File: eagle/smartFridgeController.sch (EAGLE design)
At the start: 12 parts

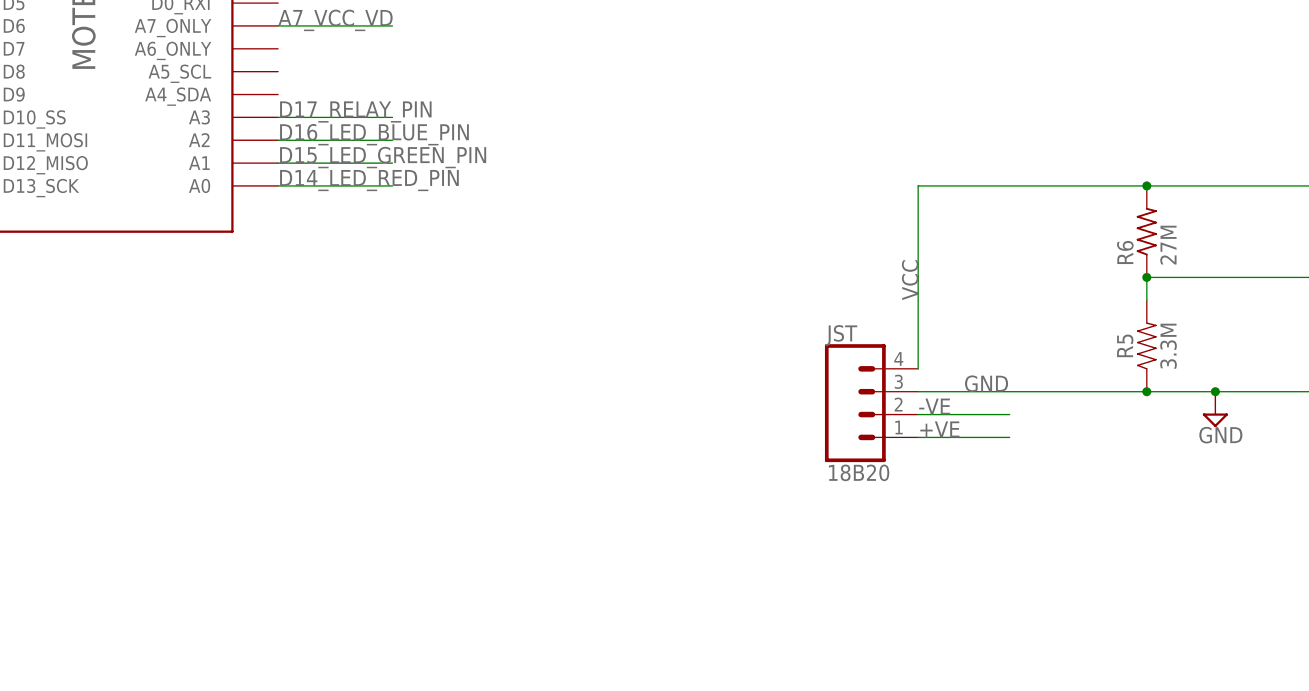
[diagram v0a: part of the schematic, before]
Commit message: gnd, vcc switch, labled switch on oki-78
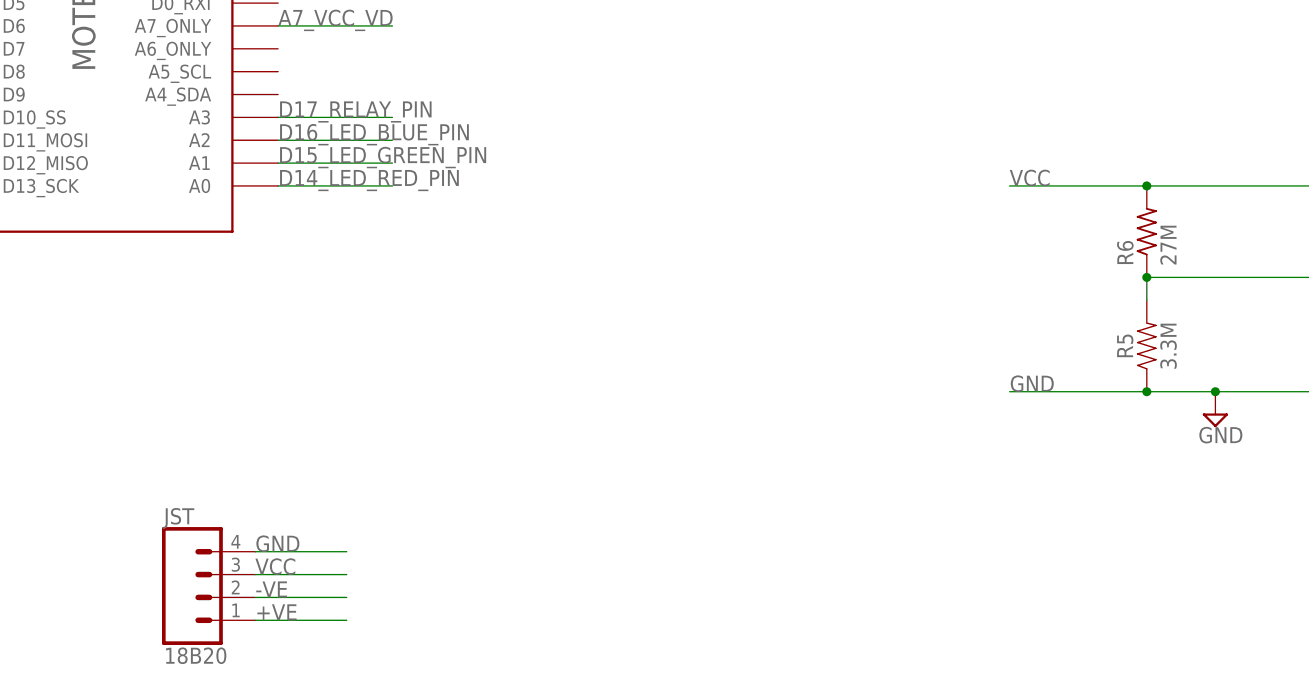
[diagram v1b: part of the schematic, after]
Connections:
- new net N$4: JST.4
- net GND: no longer JST.3
- net VCC: now also JST.3; no longer JST.4
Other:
- moved on the sheet: JST
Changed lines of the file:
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@@
 <instance part="C1" gate="G$1" x="190.5" y="50.8"/>
 <instance part="R5" gate="G$1" x="170.18" y="50.8" rot="R90"/>
-<instance part="JST" gate="G$1" x="139.7" y="43.18"/>
+<instance part="JST" gate="G$1" x="66.04" y="22.86"/>
 <instance part="R6" gate="G$1" x="170.18" y="63.5" rot="R90"/>
 <instance part="SUPPLY3" gate="GND" x="93.98" y="96.52"/>
@@
 <segment>
 <pinref part="C1" gate="G$1" pin="2"/>
-<wire x1="144.78" y1="45.72" x2="170.18" y2="45.72" width="0.1524" layer="91"/>
 <wire x1="170.18" y1="45.72" x2="177.8" y2="45.72" width="0.1524" layer="91"/>
 <wire x1="177.8" y1="45.72" x2="190.5" y2="45.72" width="0.1524" layer="91"/>
 <wire x1="190.5" y1="45.72" x2="190.5" y2="48.26" width="0.1524" layer="91"/>
-<label x="149.86" y="45.72" size="1.778" layer="95"/>
+<label x="71.12" y="27.94" size="1.778" layer="95"/>
 <pinref part="R5" gate="G$1" pin="1"/>
-<junction x="170.18" y="45.72"/>
 <pinref part="SUPPLY7" gate="GND" pin="GND"/>
 <junction x="177.8" y="45.72"/>
 <wire x1="190.5" y1="45.72" x2="231.14" y2="45.72" width="0.1524" layer="91"/>
 <junction x="190.5" y="45.72"/>
-<pinref part="JST" gate="G$1" pin="3"/>
 <pinref part="OKI-78SR-5/1.5-W36-C" gate="J$1" pin="3"/>
 <wire x1="231.14" y1="53.34" x2="231.14" y2="45.72" width="0.1524" layer="91"/>
+<wire x1="170.18" y1="45.72" x2="154.94" y2="45.72" width="0.1524" layer="91"/>
+<junction x="170.18" y="45.72"/>
+<label x="154.94" y="45.72" size="1.778" layer="95"/>
 </segment>
 <segment>
@@
 <net name="VCC" class="1">
 <segment>
-<wire x1="144.78" y1="68.58" x2="144.78" y2="48.26" width="0.1524" layer="91"/>
-<label x="144.78" y="55.88" size="1.778" layer="95" rot="R90"/>
-<pinref part="JST" gate="G$1" pin="4"/>
-<wire x1="144.78" y1="68.58" x2="170.18" y2="68.58" width="0.1524" layer="91"/>
 <pinref part="R6" gate="G$1" pin="2"/>
 <wire x1="170.18" y1="68.58" x2="223.52" y2="68.58" width="0.1524" layer="91"/>
-<junction x="170.18" y="68.58"/>
 <wire x1="223.52" y1="68.58" x2="223.52" y2="58.42" width="0.1524" layer="91"/>
 <pinref part="OKI-78SR-5/1.5-W36-C" gate="J$1" pin="1"/>
 <wire x1="223.52" y1="58.42" x2="231.14" y2="58.42" width="0.1524" layer="91"/>
+<wire x1="170.18" y1="68.58" x2="154.94" y2="68.58" width="0.1524" layer="91"/>
+<junction x="170.18" y="68.58"/>
+<label x="154.94" y="68.58" size="1.778" layer="95"/>
+</segment>
+<segment>
+<pinref part="JST" gate="G$1" pin="3"/>
+<wire x1="71.12" y1="25.4" x2="81.28" y2="25.4" width="0.1524" layer="91"/>
+<label x="71.12" y="25.4" size="1.778" layer="95"/>
 </segment>
 </net>
@@
 <segment>
 <pinref part="JST" gate="G$1" pin="1"/>
-<wire x1="144.78" y1="40.64" x2="154.94" y2="40.64" width="0.1524" layer="91"/>
-<label x="144.78" y="40.64" size="1.778" layer="95"/>
+<wire x1="71.12" y1="20.32" x2="81.28" y2="20.32" width="0.1524" layer="91"/>
+<label x="71.12" y="20.32" size="1.778" layer="95"/>
 </segment>
 <segment>
@@
 <segment>
 <pinref part="JST" gate="G$1" pin="2"/>
-<wire x1="144.78" y1="43.18" x2="154.94" y2="43.18" width="0.1524" layer="91"/>
-<label x="144.78" y="43.18" size="1.778" layer="95"/>
+<wire x1="71.12" y1="22.86" x2="81.28" y2="22.86" width="0.1524" layer="91"/>
+<label x="71.12" y="22.86" size="1.778" layer="95"/>
 </segment>
 <segment>
@@
 </segment>
 </net>
+<net name="N$4" class="0">
+<segment>
+<pinref part="JST" gate="G$1" pin="4"/>
+<wire x1="71.12" y1="27.94" x2="81.28" y2="27.94" width="0.1524" layer="91"/>
+</segment>
+</net>

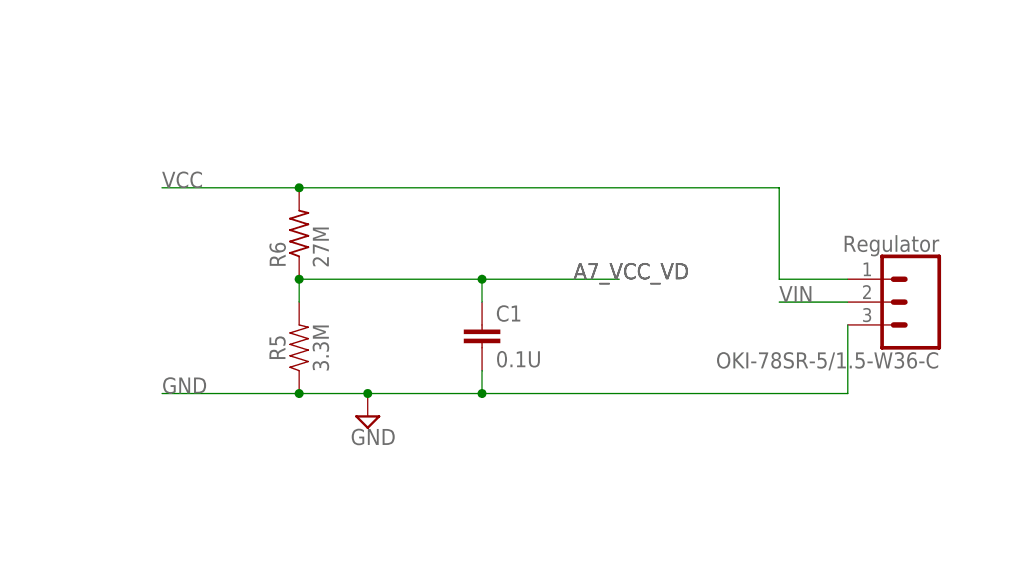
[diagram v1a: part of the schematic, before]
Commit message: silkscreen fixes, routing 0.3
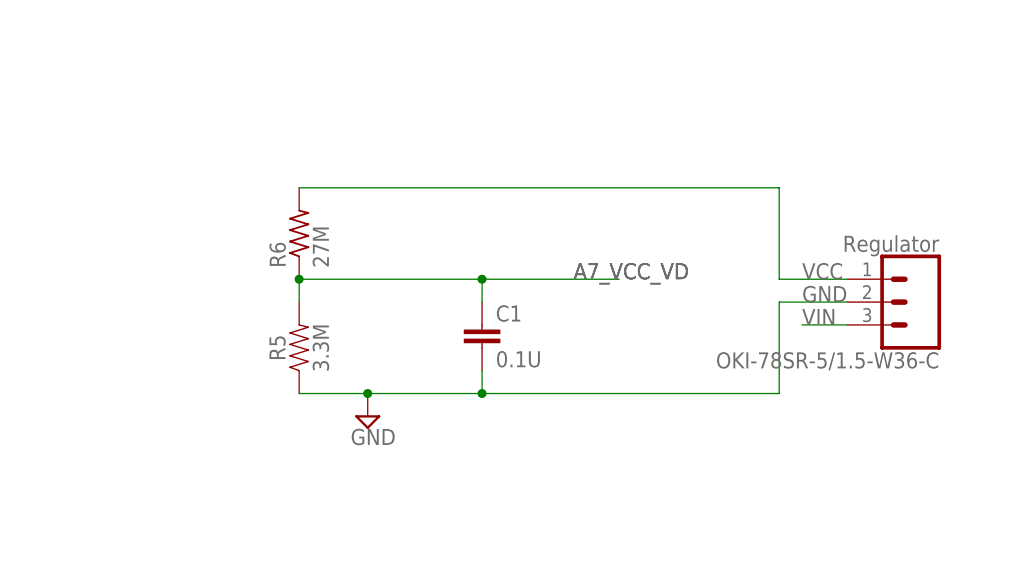
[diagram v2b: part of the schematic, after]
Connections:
- net GND: now also OKI-78SR-5/1.5-W36-C.2; no longer OKI-78SR-5/1.5-W36-C.3
- net VIN: now also OKI-78SR-5/1.5-W36-C.3; no longer OKI-78SR-5/1.5-W36-C.2
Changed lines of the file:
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@@
 <pinref part="SUPPLY7" gate="GND" pin="GND"/>
 <junction x="177.8" y="45.72"/>
-<wire x1="190.5" y1="45.72" x2="231.14" y2="45.72" width="0.1524" layer="91"/>
+<wire x1="190.5" y1="45.72" x2="223.52" y2="45.72" width="0.1524" layer="91"/>
+<wire x1="223.52" y1="45.72" x2="223.52" y2="55.88" width="0.1524" layer="91"/>
 <junction x="190.5" y="45.72"/>
-<pinref part="OKI-78SR-5/1.5-W36-C" gate="J$1" pin="3"/>
-<wire x1="231.14" y1="53.34" x2="231.14" y2="45.72" width="0.1524" layer="91"/>
-<wire x1="170.18" y1="45.72" x2="154.94" y2="45.72" width="0.1524" layer="91"/>
-<junction x="170.18" y="45.72"/>
-<label x="154.94" y="45.72" size="1.778" layer="95"/>
+<pinref part="OKI-78SR-5/1.5-W36-C" gate="J$1" pin="2"/>
+<wire x1="223.52" y1="55.88" x2="231.14" y2="55.88" width="0.1524" layer="91"/>
+<label x="226.06" y="55.88" size="1.778" layer="95"/>
 </segment>
 <segment>
@@
 </segment>
 <segment>
-<pinref part="OKI-78SR-5/1.5-W36-C" gate="J$1" pin="2"/>
-<wire x1="231.14" y1="55.88" x2="223.52" y2="55.88" width="0.1524" layer="91"/>
-<label x="223.52" y="55.88" size="1.778" layer="95"/>
+<pinref part="OKI-78SR-5/1.5-W36-C" gate="J$1" pin="3"/>
+<wire x1="231.14" y1="53.34" x2="226.06" y2="53.34" width="0.1524" layer="91"/>
+<label x="226.06" y="53.34" size="1.778" layer="95"/>
 </segment>
 </net>
@@
 <pinref part="OKI-78SR-5/1.5-W36-C" gate="J$1" pin="1"/>
 <wire x1="223.52" y1="58.42" x2="231.14" y2="58.42" width="0.1524" layer="91"/>
-<wire x1="170.18" y1="68.58" x2="154.94" y2="68.58" width="0.1524" layer="91"/>
-<junction x="170.18" y="68.58"/>
-<label x="154.94" y="68.58" size="1.778" layer="95"/>
+<label x="226.06" y="58.42" size="1.778" layer="95"/>
 </segment>
 <segment>

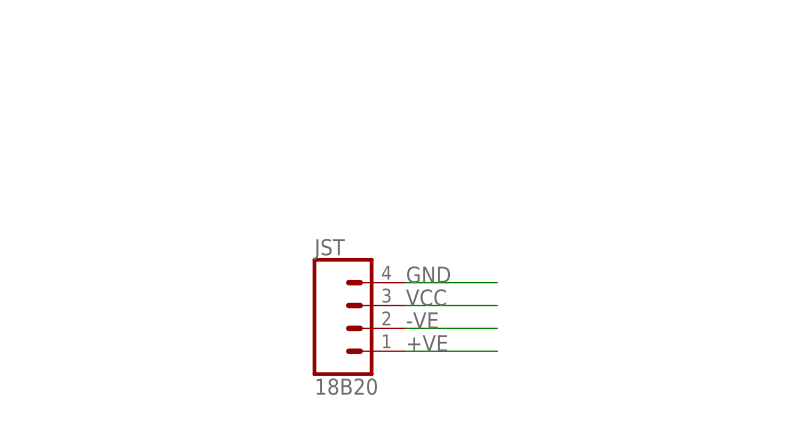
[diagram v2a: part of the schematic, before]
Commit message: Moved to screwterminal(s)
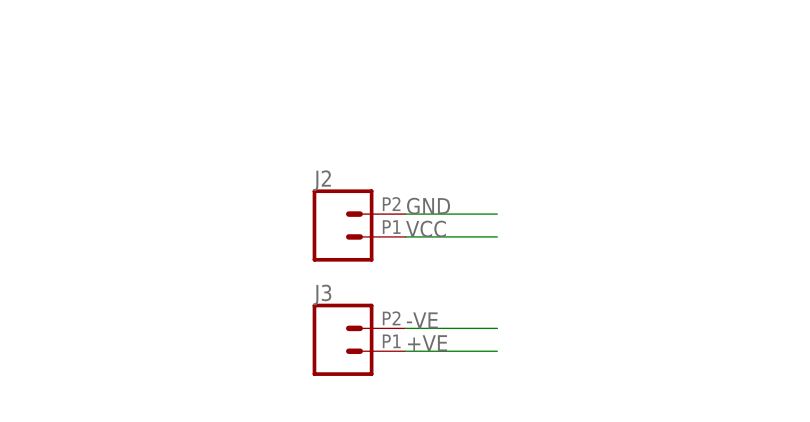
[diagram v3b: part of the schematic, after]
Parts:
- removed JST: 18B20, SparkFun-Connectors:CONN_04JST-PTH
- added J2, J3: (no value), SparkFun-Connectors:CONN_022.54MM_SCREWTERM
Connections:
- removed net N$4: JST.4
- net +VE: now also J3.1; no longer JST.1
- net -VE: now also J3.2; no longer JST.2
- net GND: now also J2.2
- net VCC: now also J2.1; no longer JST.3
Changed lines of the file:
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@@
 <part name="C1" library="SparkFun-Capacitors" deviceset="0.1UF" device="-KIT-EZ-50V-20%" value="0.1U"/>
 <part name="R5" library="SparkFun-Resistors" deviceset="1KOHM" device="-HORIZ-1/4W-1%" value="3.3M"/>
-<part name="JST" library="SparkFun-Connectors" deviceset="CONN_04" device="JST-PTH" value="18B20"/>
 <part name="R6" library="adafruit" deviceset="R-US_" device="0309/12" value="27M"/>
 <part name="SUPPLY3" library="supply2" deviceset="GND" device=""/>
@@
 <part name="IXYS_CPC_1706Y" library="relay" library_urn="urn:adsk.eagle:library:339" deviceset="AQZ10*D" device="" package3d_urn="urn:adsk.eagle:package:24370/1" technology="2"/>
 <part name="STATUS_LED" library="SparkFun-LED" deviceset="LED-RGB-CA" device="CLEAR" value="CLEAR"/>
+<part name="J2" library="SparkFun-Connectors" deviceset="CONN_02" device="2.54MM_SCREWTERM"/>
+<part name="J3" library="SparkFun-Connectors" deviceset="CONN_02" device="2.54MM_SCREWTERM"/>
 </parts>
 <sheets>
@@
 <instance part="C1" gate="G$1" x="190.5" y="50.8"/>
 <instance part="R5" gate="G$1" x="170.18" y="50.8" rot="R90"/>
-<instance part="JST" gate="G$1" x="66.04" y="22.86"/>
 <instance part="R6" gate="G$1" x="170.18" y="63.5" rot="R90"/>
 <instance part="SUPPLY3" gate="GND" x="93.98" y="96.52"/>
@@
 </instance>
 <instance part="STATUS_LED" gate="G$1" x="215.9" y="134.62"/>
+<instance part="J2" gate="G$1" x="63.5" y="33.02"/>
+<instance part="J3" gate="G$1" x="63.5" y="20.32"/>
 </instances>
 <busses>
@@
 <wire x1="177.8" y1="45.72" x2="190.5" y2="45.72" width="0.1524" layer="91"/>
 <wire x1="190.5" y1="45.72" x2="190.5" y2="48.26" width="0.1524" layer="91"/>
-<label x="71.12" y="27.94" size="1.778" layer="95"/>
 <pinref part="R5" gate="G$1" pin="1"/>
 <pinref part="SUPPLY7" gate="GND" pin="GND"/>
@@
 <label x="228.6" y="134.62" size="1.778" layer="95"/>
 </segment>
+<segment>
+<pinref part="J2" gate="G$1" pin="2"/>
+<wire x1="71.12" y1="35.56" x2="81.28" y2="35.56" width="0.1524" layer="91"/>
+<label x="71.12" y="35.56" size="1.778" layer="95"/>
+</segment>
 </net>
 <net name="VIN" class="1">
@@
 </segment>
 <segment>
-<pinref part="JST" gate="G$1" pin="3"/>
-<wire x1="71.12" y1="25.4" x2="81.28" y2="25.4" width="0.1524" layer="91"/>
-<label x="71.12" y="25.4" size="1.778" layer="95"/>
+<pinref part="J2" gate="G$1" pin="1"/>
+<wire x1="71.12" y1="33.02" x2="81.28" y2="33.02" width="0.1524" layer="91"/>
+<label x="71.12" y="33.02" size="1.778" layer="95"/>
 </segment>
 </net>
 <net name="+VE" class="1">
 <segment>
-<pinref part="JST" gate="G$1" pin="1"/>
 <wire x1="71.12" y1="20.32" x2="81.28" y2="20.32" width="0.1524" layer="91"/>
 <label x="71.12" y="20.32" size="1.778" layer="95"/>
+<pinref part="J3" gate="G$1" pin="1"/>
 </segment>
 <segment>
@@
 <net name="-VE" class="1">
 <segment>
-<pinref part="JST" gate="G$1" pin="2"/>
 <wire x1="71.12" y1="22.86" x2="81.28" y2="22.86" width="0.1524" layer="91"/>
 <label x="71.12" y="22.86" size="1.778" layer="95"/>
+<pinref part="J3" gate="G$1" pin="2"/>
 </segment>
 <segment>
@@
 </segment>
 </net>
-<net name="N$4" class="0">
-<segment>
-<pinref part="JST" gate="G$1" pin="4"/>
-<wire x1="71.12" y1="27.94" x2="81.28" y2="27.94" width="0.1524" layer="91"/>
-</segment>
-</net>
